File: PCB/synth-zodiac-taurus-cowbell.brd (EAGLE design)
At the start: 76.1 x 72.4 mm, 67 parts, among them Q1 NPN, Q2 NPN, U1 TL071, U3 ATmega328P-AU, X1 16MHz, X2 16MHz, X3 16MHz

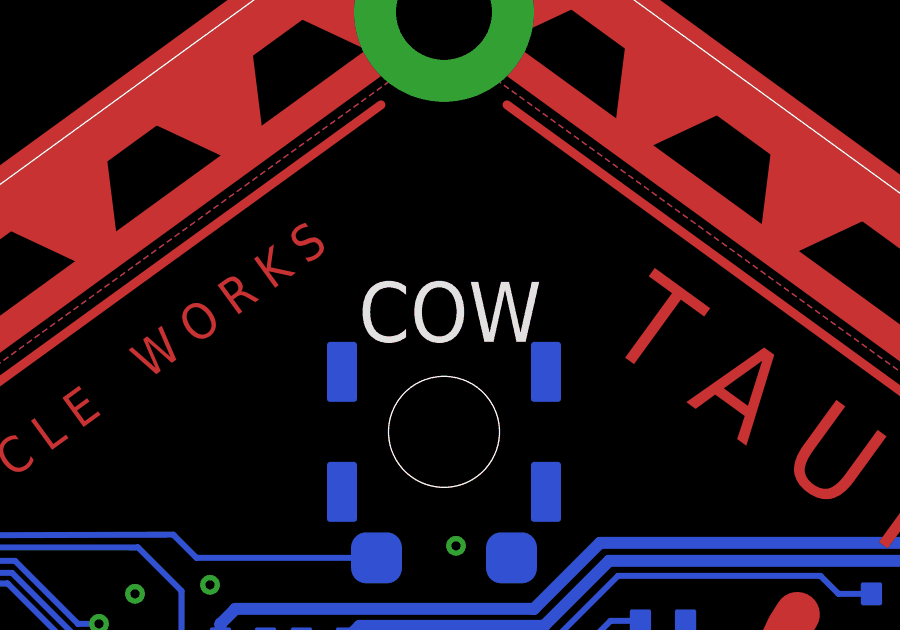
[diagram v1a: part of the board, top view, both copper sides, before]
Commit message: Tune values and some schematic visual tweaks.
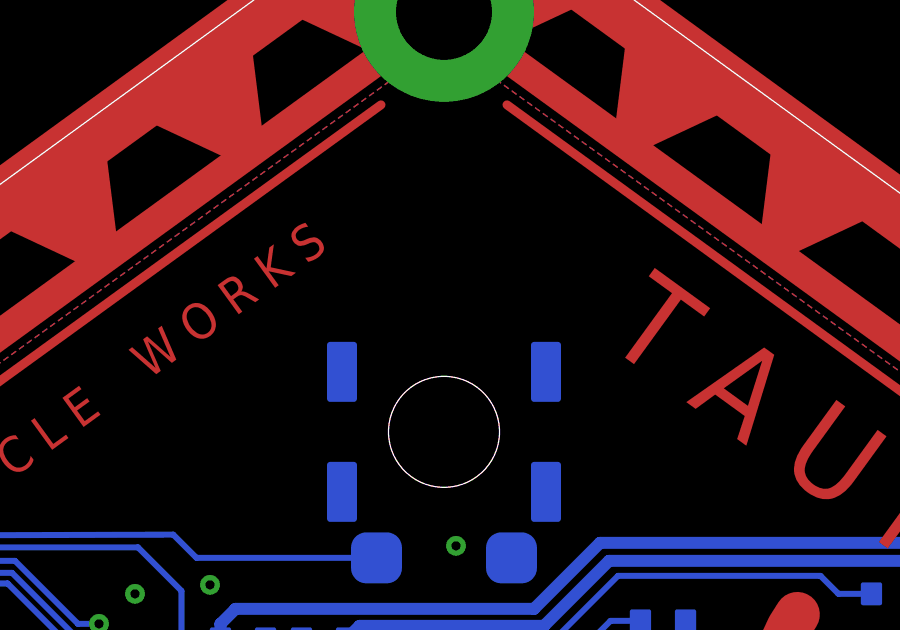
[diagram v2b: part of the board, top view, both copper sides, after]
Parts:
- ICSP: value Connector, 6P, SM, VT -> Connector, 6P, SH, VT
- R13: value 33K -> 10K
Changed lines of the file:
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@@
 <attribute name="VALUE" x="21.6" y="30.3" size="0.2" layer="28" rot="MR180" align="center"/>
 </element>
-<element name="R13" library="rlc" library_urn="urn:adsk.eagle:library:4192893" package="0603-RES" package3d_urn="urn:adsk.eagle:package:4193040/5" value="33K" x="40.5" y="17.7" smashed="yes" rot="MR0">
+<element name="R13" library="rlc" library_urn="urn:adsk.eagle:library:4192893" package="0603-RES" package3d_urn="urn:adsk.eagle:package:4193040/5" value="10K" x="40.5" y="17.7" smashed="yes" rot="MR0">
 <attribute name="COST01" value="0.10" x="40.5" y="17.7" size="1.778" layer="28" rot="MR0" display="off"/>
 <attribute name="COST10" value="0.05" x="40.5" y="17.7" size="1.778" layer="28" rot="MR0" display="off"/>
@@
 <attribute name="MPN" value="B3FS" x="38" y="54" size="1.778" layer="27" rot="R270" display="off"/>
 <attribute name="MPN2" value="Tayda A-3961(2.3mm), A-5134(3.14mm,RA)" x="38" y="54" size="1.778" layer="27" rot="R270" display="off"/>
+<attribute name="NAME" x="38.2" y="58" size="2" layer="25" font="vector" ratio="15" rot="SR0" align="center"/>
 <attribute name="NAME" x="38.053" y="49.383" size="0.7" layer="26" font="vector" ratio="15" rot="SMR0" align="center"/>
-<attribute name="NAME" x="38.2" y="58" size="2" layer="25" font="vector" ratio="15" rot="SR0" align="center"/>
 <attribute name="VALUE" x="35.189" y="54" size="0.3" layer="27" font="vector" rot="R270" align="center"/>
 </element>
@@
 </element>
 <element name="GLYPH1" library="circuit-monkey-zodiac" library_urn="urn:adsk.eagle:library:36060312" package="TAURUS-GLYPH" package3d_urn="urn:adsk.eagle:package:41522816/2" value="" x="48.9" y="39.9" smashed="yes" rot="R324"/>
-<element name="ICSP" library="con-jst" library_urn="urn:adsk.eagle:library:7191852" package="BM06B-SRSS-TB" package3d_urn="urn:adsk.eagle:package:41517274/3" value="Connector, 6P, SM, VT" x="37.8" y="12.1" smashed="yes" rot="MR180">
+<element name="ICSP" library="con-jst" library_urn="urn:adsk.eagle:library:7191852" package="BM06B-SRSS-TB" package3d_urn="urn:adsk.eagle:package:41517274/3" value="Connector, 6P, SH, VT" x="37.8" y="12.1" smashed="yes" rot="MR180">
 <attribute name="COST01" value="0.60" x="37.8" y="12.1" size="1.778" layer="28" rot="MR180" display="off"/>
 <attribute name="COST10" value="0.52" x="37.8" y="12.1" size="1.778" layer="28" rot="MR180" display="off"/>
